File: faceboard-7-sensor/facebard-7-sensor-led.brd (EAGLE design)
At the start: 37 x 91.4 mm, 31 parts, among them Q1 QRE1113, Q2 QRE1113, Q3 QRE1113, Q4 QRE1113, Q5 QRE1113, Q6 QRE1113, Q7 QRE1113, U1 CD4051BE

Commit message: routing
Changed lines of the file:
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@@
 <signal name="C0">
 <contactref element="U1" pad="13"/>
+<wire x1="15.18" y1="7" x2="15.18" y2="19.46894375" width="0.1524" layer="16"/>
+<wire x1="16.6659" y1="20.95484375" x2="15.18" y2="19.46894375" width="0.1524" layer="16"/>
+<wire x1="15.18" y1="43.47" x2="15.18" y2="42.16928125" width="0.1524" layer="16"/>
+<wire x1="15.18" y1="42.16928125" x2="16.6659" y2="40.68338125" width="0.1524" layer="16"/>
+<wire x1="16.6659" y1="40.68338125" x2="16.6659" y2="20.95484375" width="0.1524" layer="16"/>
 <contactref element="Q1" pad="3"/>
 <contactref element="R2" pad="1"/>
 <wire x1="5.515" y1="3.5134" x2="8.5066" y2="3.5134" width="0.1524" layer="1"/>
 <wire x1="8.5066" y1="3.5134" x2="10.1" y2="1.92" width="0.1524" layer="1"/>
-<wire x1="15.18" y1="7" x2="10.1" y2="1.92" width="0.1524" layer="16"/>
-<wire x1="15.18" y1="19.46894375" x2="15.18" y2="7" width="0.1524" layer="16"/>
-<wire x1="16.6659" y1="20.95484375" x2="15.18" y2="19.46894375" width="0.1524" layer="16"/>
-<wire x1="15.18" y1="43.47" x2="15.18" y2="42.16928125" width="0.1524" layer="16"/>
-<wire x1="15.18" y1="42.16928125" x2="16.6659" y2="40.68338125" width="0.1524" layer="16"/>
-<wire x1="16.6659" y1="40.68338125" x2="16.6659" y2="20.95484375" width="0.1524" layer="16"/>
+<wire x1="10.1" y1="1.92" x2="15.18" y2="7" width="0.1524" layer="16"/>
 </signal>
 <signal name="GND">
@@
 </signal>
 <signal name="C1">
+<contactref element="U1" pad="14"/>
+<wire x1="15.18" y1="40.93" x2="15.18" y2="39.62928125" width="0.1524" layer="16"/>
+<wire x1="15.18" y1="39.62928125" x2="16.3611" y2="38.44818125" width="0.1524" layer="16"/>
+<wire x1="16.3611" y1="21.0811" x2="16.3611" y2="38.44818125" width="0.1524" layer="16"/>
 <contactref element="Q2" pad="3"/>
 <contactref element="R4" pad="1"/>
-<contactref element="U1" pad="14"/>
 <wire x1="5.515" y1="17.5334" x2="7.3394" y2="15.709" width="0.1524" layer="1"/>
 <wire x1="7.3394" y1="15.709" x2="7.8682375" y2="15.709" width="0.1524" layer="1"/>
 <wire x1="8.7572375" y1="14.82" x2="10.1" y2="14.82" width="0.1524" layer="1"/>
 <wire x1="7.8682375" y1="15.709" x2="8.7572375" y2="14.82" width="0.1524" layer="1"/>
-<wire x1="15.18" y1="40.93" x2="15.18" y2="39.62928125" width="0.1524" layer="16"/>
-<wire x1="15.18" y1="39.62928125" x2="16.3611" y2="38.44818125" width="0.1524" layer="16"/>
-<wire x1="16.3611" y1="38.44818125" x2="16.3611" y2="21.0811" width="0.1524" layer="16"/>
-<wire x1="16.3611" y1="21.0811" x2="10.1" y2="14.82" width="0.1524" layer="16"/>
+<wire x1="10.1" y1="14.82" x2="16.3611" y2="21.0811" width="0.1524" layer="16"/>
 </signal>
 <signal name="N$5">
@@
 </signal>
 <signal name="C2">
+<contactref element="U1" pad="15"/>
+<wire x1="15.18" y1="38.39" x2="15.18" y2="37.08928125" width="0.1524" layer="16"/>
+<wire x1="15.18" y1="37.08928125" x2="16.0563" y2="36.21298125" width="0.1524" layer="16"/>
+<wire x1="16.0563" y1="36.21298125" x2="16.0563" y2="34" width="0.1524" layer="16"/>
 <contactref element="Q3" pad="3"/>
 <contactref element="R6" pad="1"/>
-<contactref element="U1" pad="15"/>
+<wire x1="16.0563" y1="34" x2="16.0563" y2="33.6763" width="0.1524" layer="16"/>
 <wire x1="5.515" y1="31.5534" x2="9.3484" y2="27.72" width="0.1524" layer="1"/>
 <wire x1="9.3484" y1="27.72" x2="10.1" y2="27.72" width="0.1524" layer="1"/>
-<wire x1="15.18" y1="38.39" x2="15.18" y2="37.08928125" width="0.1524" layer="16"/>
-<wire x1="15.18" y1="37.08928125" x2="16.0563" y2="36.21298125" width="0.1524" layer="16"/>
-<wire x1="16.0563" y1="36.21298125" x2="16.0563" y2="33.6763" width="0.1524" layer="16"/>
-<wire x1="16.0563" y1="33.6763" x2="10.1" y2="27.72" width="0.1524" layer="16"/>
+<wire x1="16.0563" y1="33.6763" x2="16.0563" y2="33.0563" width="0.1524" layer="16"/>
+<wire x1="10.72" y1="27.72" x2="10.1" y2="27.72" width="0.1524" layer="16"/>
+<wire x1="16.0563" y1="33.0563" x2="10.72" y2="27.72" width="0.1524" layer="16"/>
 </signal>
 <signal name="N$7">
@@
 </signal>
 <signal name="C3">
+<contactref element="U1" pad="12"/>
 <contactref element="Q4" pad="3"/>
 <contactref element="R8" pad="1"/>
-<contactref element="U1" pad="12"/>
-<wire x1="5.515" y1="45.5734" x2="10.1" y2="40.9884" width="0.1524" layer="1"/>
-<wire x1="10.1" y1="40.9884" x2="10.1" y2="40.62" width="0.1524" layer="1"/>
 <wire x1="15.18" y1="46.01" x2="10.1" y2="40.93" width="0.1524" layer="16"/>
 <wire x1="10.1" y1="40.93" x2="10.1" y2="40.62" width="0.1524" layer="16"/>
+<wire x1="10.1" y1="40.62" x2="5.515" y2="45.205" width="0.1524" layer="1"/>
+<wire x1="5.515" y1="45.205" x2="5.515" y2="45.5734" width="0.1524" layer="1"/>
 </signal>
 <signal name="N$9">
@@
 <contactref element="Q5" pad="3"/>
 <contactref element="R10" pad="1"/>
-<contactref element="U1" pad="1"/>
 <wire x1="5.515" y1="59.5934" x2="10.1" y2="55.0084" width="0.1524" layer="1"/>
 <wire x1="10.1" y1="55.0084" x2="10.1" y2="53.52" width="0.1524" layer="1"/>
-<wire x1="22.8" y1="35.85" x2="16.0563" y2="42.5937" width="0.1524" layer="16"/>
-<wire x1="10.1" y1="52.32928125" x2="10.1" y2="53" width="0.1524" layer="16"/>
-<wire x1="10.1" y1="53" x2="10.1" y2="53.52" width="0.1524" layer="16"/>
-<wire x1="16.0563" y1="42.5937" x2="16.0563" y2="46" width="0.1524" layer="16"/>
-<wire x1="16.0563" y1="46" x2="16.0563" y2="46.37298125" width="0.1524" layer="16"/>
+<wire x1="10.1" y1="52.0372375" x2="10.1" y2="53.52" width="0.1524" layer="16"/>
+<wire x1="16.0563" y1="42.5937" x2="16.0563" y2="46.37298125" width="0.1524" layer="16"/>
 <wire x1="16.0563" y1="46.37298125" x2="15.54298125" y2="46.8863" width="0.1524" layer="16"/>
 <wire x1="15.54298125" y1="46.8863" x2="15.1733625" y2="46.8863" width="0.1524" layer="16"/>
 <wire x1="15.1733625" y1="46.8863" x2="10.989" y2="51.0706625" width="0.1524" layer="16"/>
 <wire x1="10.989" y1="51.0706625" x2="10.989" y2="51.1482375" width="0.1524" layer="16"/>
-<wire x1="10.1" y1="52.0372375" x2="10.1" y2="52.32928125" width="0.1524" layer="16"/>
 <wire x1="10.989" y1="51.1482375" x2="10.1" y2="52.0372375" width="0.1524" layer="16"/>
+<contactref element="U1" pad="1"/>
+<wire x1="22.8" y1="35.85" x2="16.0563" y2="42.5937" width="0.1524" layer="16"/>
 </signal>
 <signal name="N$11">
@@
 <contactref element="Q6" pad="3"/>
 <contactref element="R12" pad="1"/>
-<contactref element="U1" pad="5"/>
 <wire x1="5.515" y1="73.6134" x2="10.1" y2="69.0284" width="0.1524" layer="1"/>
 <wire x1="10.1" y1="69.0284" x2="10.1" y2="66.42" width="0.1524" layer="1"/>
-<wire x1="22.8" y1="46.01" x2="19.3048" y2="49.5052" width="0.1524" layer="1"/>
 <wire x1="14" y1="56.04928125" x2="14" y2="63" width="0.1524" layer="1"/>
 <wire x1="19.3048" y1="49.5052" x2="19.3048" y2="50.74448125" width="0.1524" layer="1"/>
@@
 <wire x1="14" y1="63" x2="10.58" y2="66.42" width="0.1524" layer="1"/>
 <wire x1="10.58" y1="66.42" x2="10.1" y2="66.42" width="0.1524" layer="1"/>
+<contactref element="U1" pad="5"/>
+<wire x1="22.8" y1="46.01" x2="19.3048" y2="49.5052" width="0.1524" layer="1"/>
 </signal>
 <signal name="N$13">
@@
 </signal>
 <signal name="C6">
-<contactref element="Q7" pad="3"/>
-<contactref element="R14" pad="1"/>
 <contactref element="U1" pad="2"/>
-<wire x1="5.515" y1="87.6334" x2="10.1" y2="83.0484" width="0.1524" layer="1"/>
-<wire x1="10.1" y1="83.0484" x2="10.1" y2="79.32" width="0.1524" layer="1"/>
 <wire x1="22.8" y1="38.39" x2="16.3611" y2="44.8289" width="0.1524" layer="16"/>
 <wire x1="16.3611" y1="44.8289" x2="16.3611" y2="46.4992375" width="0.1524" layer="16"/>
 <wire x1="16" y1="46.8603375" x2="16" y2="47" width="0.1524" layer="16"/>
 <wire x1="16.3611" y1="46.4992375" x2="16" y2="46.8603375" width="0.1524" layer="16"/>
-<wire x1="11.9989" y1="77.4211" x2="10.1" y2="79.32" width="0.1524" layer="16"/>
 <wire x1="16" y1="47" x2="15.3263" y2="47.6737" width="0.1524" layer="16"/>
 <wire x1="15.3263" y1="47.6737" x2="14.81701875" y2="47.6737" width="0.1524" layer="16"/>
 <wire x1="14.81701875" y1="47.6737" x2="11.9989" y2="50.49181875" width="0.1524" layer="16"/>
-<wire x1="11.9989" y1="50.49181875" x2="11.9989" y2="77.4211" width="0.1524" layer="16"/>
+<wire x1="11.9989" y1="50.49181875" x2="11.9989" y2="77" width="0.1524" layer="16"/>
+<contactref element="Q7" pad="3"/>
+<contactref element="R14" pad="1"/>
+<wire x1="5.515" y1="87.6334" x2="10.1" y2="83.0484" width="0.1524" layer="1"/>
+<wire x1="10.1" y1="83.0484" x2="10.1" y2="79.32" width="0.1524" layer="1"/>
+<wire x1="11.9989" y1="77" x2="11.9989" y2="77.4211" width="0.1524" layer="16"/>
+<wire x1="11.9989" y1="77.4211" x2="10.1" y2="79.32" width="0.1524" layer="16"/>
 </signal>
 <signal name="SIG">

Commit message: re-draw schematics
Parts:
- R10: value 10k -> 100k
- SV2: value header -> Output
- SV3: value header -> Input
- moved U1 6.60 mm to (17.0, 39.0), flipped to the bottom
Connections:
- net LEDDIN renamed N$12
- new net N$14: D1.1, D2.1, D3.1
- new net N$15: D4.1
- new net VCC: R1.1, R10.2, R11.1, R12.2, R13.1, R14.2, R2.2, R3.1, R4.2, R5.1, R6.2, R7.1, R8.2, R9.1, SV2.2, SV3.2
- net 5V: no longer R1.1, R10.2, R11.1, R12.2, R13.1, R14.2, R2.2, R3.1, R4.2, R5.1, R6.2, R7.1, R8.2, R9.1, SV2.2, SV3.2
- net GND: no longer D1.1, D2.1, D3.1, D4.1
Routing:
- net 5V: track 127.1 -> 0.00 mm
- net 3V: track 124.5 -> 33.5 mm
- net VCC: track 0.00 -> 88.1 mm
- net C: track 95.5 -> 69.2 mm
- net C4: track 31.1 -> 21.6 mm
- net C6: track 56.7 -> 47.6 mm
- net N$6: track 8.43 -> 0.00 mm
- net N$2: track 8.43 -> 0.00 mm
- net N$8: track 8.43 -> 0.00 mm
- net N$4: track 8.43 -> 0.00 mm
- net N$10: track 8.43 -> 0.00 mm
- net C3: track 14.3 -> 7.16 mm
- net C5: track 35.0 -> 30.1 mm
- net N$12: track 4.69 -> 0.00 mm
- net B: track 97.5 -> 93.7 mm
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
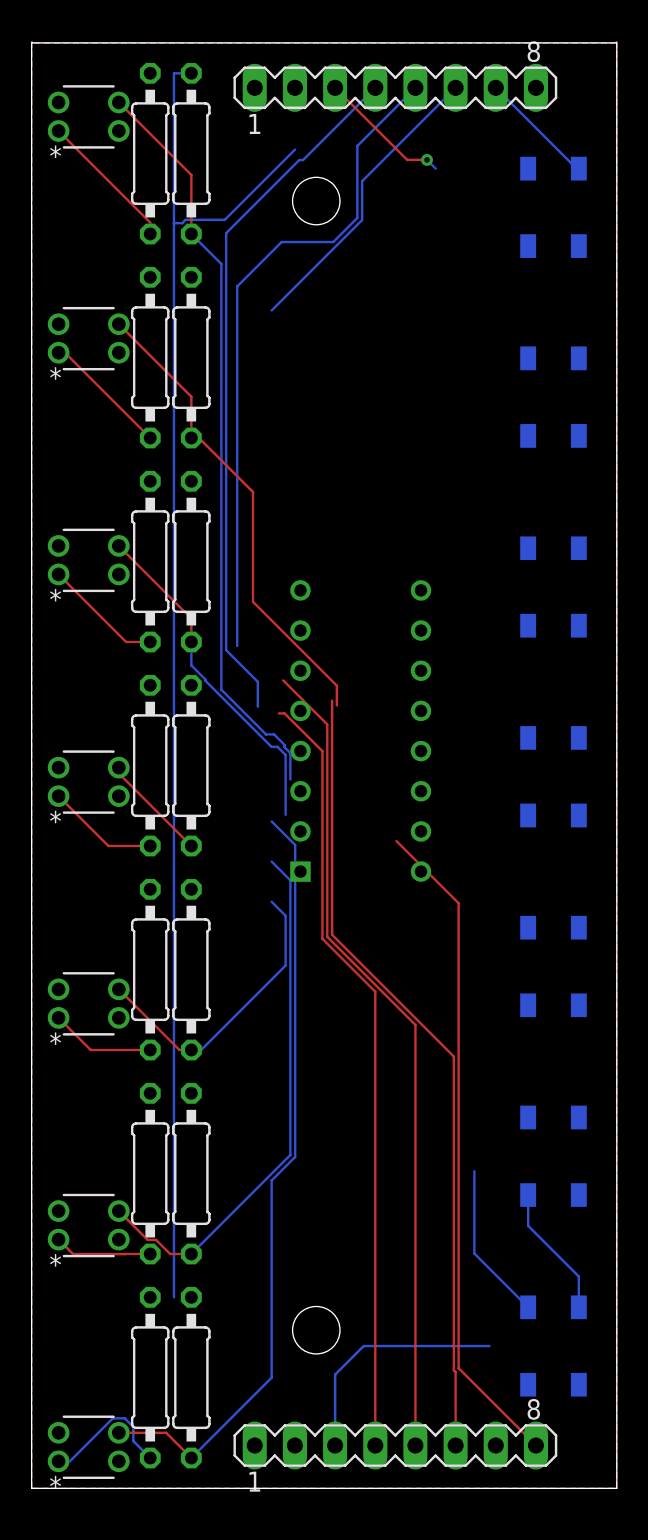
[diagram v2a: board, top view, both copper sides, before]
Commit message: fix vcc net
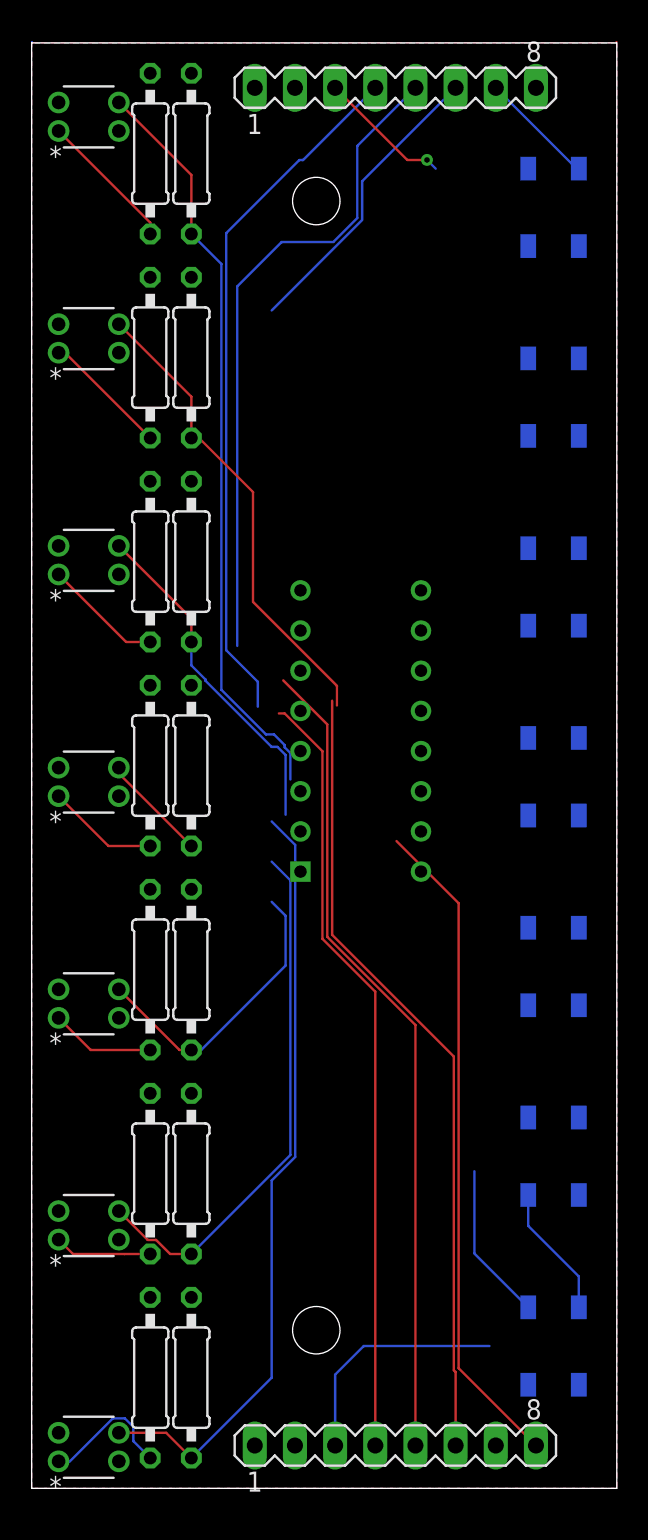
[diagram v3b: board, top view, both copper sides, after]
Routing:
- net VCC: track 88.1 -> 0.00 mm
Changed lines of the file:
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@@
 </signal>
 <signal name="VCC">
+<contactref element="SV3" pad="2"/>
+<contactref element="SV2" pad="2"/>
 <contactref element="R1" pad="1"/>
 <contactref element="R2" pad="2"/>
@@
 <contactref element="R6" pad="2"/>
 <contactref element="R7" pad="1"/>
+<contactref element="R8" pad="2"/>
+<contactref element="R9" pad="1"/>
+<contactref element="R10" pad="2"/>
+<contactref element="R11" pad="1"/>
+<contactref element="R12" pad="2"/>
+<contactref element="R13" pad="1"/>
 <contactref element="R14" pad="2"/>
-<contactref element="R13" pad="1"/>
-<contactref element="R12" pad="2"/>
-<contactref element="R11" pad="1"/>
-<contactref element="R10" pad="2"/>
-<contactref element="R9" pad="1"/>
-<contactref element="R8" pad="2"/>
-<wire x1="9" y1="89.48" x2="10.1" y2="89.48" width="0.1524" layer="16"/>
-<wire x1="9" y1="12.08" x2="9" y2="24.98" width="0.1524" layer="16"/>
-<wire x1="9" y1="24.98" x2="9" y2="37.88" width="0.1524" layer="16"/>
-<wire x1="9" y1="37.88" x2="9" y2="50.78" width="0.1524" layer="16"/>
-<wire x1="9" y1="50.78" x2="9" y2="63.68" width="0.1524" layer="16"/>
-<wire x1="9" y1="63.68" x2="9" y2="76.58" width="0.1524" layer="16"/>
-<wire x1="9" y1="76.58" x2="9" y2="80" width="0.1524" layer="16"/>
-<wire x1="9" y1="80" x2="9" y2="89.48" width="0.1524" layer="16"/>
-<wire x1="9.7317625" y1="80.209" x2="9.5227625" y2="80" width="0.1524" layer="16"/>
-<wire x1="9.5227625" y1="80" x2="9" y2="80" width="0.1524" layer="16"/>
-<wire x1="12.209" y1="80.209" x2="9.7317625" y2="80.209" width="0.1524" layer="16"/>
-<wire x1="16.65" y1="84.65" x2="12.209" y2="80.209" width="0.1524" layer="16"/>
-<contactref element="SV3" pad="2"/>
-<contactref element="SV2" pad="2"/>
-<wire x1="16.65" y1="84.65" x2="16.65" y2="88.56" width="0" layer="19" extent="16-16"/>
-<wire x1="10.1" y1="12.08" x2="9" y2="12.08" width="0" layer="19" extent="16-16"/>
-<wire x1="7.5" y1="12.08" x2="9" y2="12.08" width="0" layer="19" extent="16-16"/>
+<wire x1="10.1" y1="89.48" x2="16.65" y2="88.56" width="0" layer="19" extent="1-1"/>
 <wire x1="7.5" y1="89.48" x2="10.1" y2="89.48" width="0" layer="19" extent="1-1"/>
-<wire x1="10.1" y1="76.58" x2="16.65" y2="84.65" width="0" layer="19" extent="16-16"/>
+<wire x1="10.1" y1="76.58" x2="10.1" y2="89.48" width="0" layer="19" extent="1-1"/>
 <wire x1="7.5" y1="76.58" x2="10.1" y2="76.58" width="0" layer="19" extent="1-1"/>
-<wire x1="16.65" y1="2.71" x2="10.1" y2="12.08" width="0" layer="19" extent="1-1"/>
 <wire x1="10.1" y1="63.68" x2="10.1" y2="76.58" width="0" layer="19" extent="1-1"/>
 <wire x1="7.5" y1="63.68" x2="10.1" y2="63.68" width="0" layer="19" extent="1-1"/>
@@
 <wire x1="10.1" y1="37.88" x2="10.1" y2="50.78" width="0" layer="19" extent="1-1"/>
 <wire x1="7.5" y1="37.88" x2="10.1" y2="37.88" width="0" layer="19" extent="1-1"/>
-<wire x1="10.1" y1="24.98" x2="10.1" y2="12.08" width="0" layer="19" extent="1-1"/>
+<wire x1="10.1" y1="24.98" x2="10.1" y2="37.88" width="0" layer="19" extent="1-1"/>
 <wire x1="7.5" y1="24.98" x2="10.1" y2="24.98" width="0" layer="19" extent="1-1"/>
+<wire x1="10.1" y1="12.08" x2="10.1" y2="24.98" width="0" layer="19" extent="1-1"/>
+<wire x1="7.5" y1="12.08" x2="10.1" y2="12.08" width="0" layer="19" extent="1-1"/>
+<wire x1="16.65" y1="2.71" x2="10.1" y2="12.08" width="0" layer="19" extent="1-1"/>
 </signal>
 <signal name="N$15">

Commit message: add din dout labels
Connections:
- net LEDDOUT renamed DOUT
- net N$12 renamed DIN
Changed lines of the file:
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@@
 <wire x1="31.4" y1="16.6" x2="34.6" y2="13.4" width="0.1524" layer="16"/>
 </signal>
-<signal name="LEDDOUT">
+<signal name="DOUT">
 <contactref element="D7" pad="4"/>
 <contactref element="SV2" pad="7"/>
@@
 <wire x1="34.6" y1="47.45" x2="31.4" y2="54.55" width="0" layer="19" extent="16-16"/>
 </signal>
-<signal name="N$12">
+<signal name="DIN">
 <contactref element="D1" pad="2"/>
 <contactref element="SV3" pad="7"/>

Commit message: tidy
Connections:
- removed net 5V: U1.16
- net VCC: now also U1.16
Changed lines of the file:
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@@
 <contactref element="SV2" pad="8"/>
-</signal>
-<signal name="5V">
-<contactref element="U1" pad="16"/>
 </signal>
 <signal name="A">
@@
 <contactref element="R13" pad="1"/>
 <contactref element="R14" pad="2"/>
+<contactref element="U1" pad="16"/>
 <wire x1="10.1" y1="89.48" x2="16.65" y2="88.56" width="0" layer="19" extent="1-1"/>
 <wire x1="7.5" y1="89.48" x2="10.1" y2="89.48" width="0" layer="19" extent="1-1"/>
@@
 <wire x1="7.5" y1="12.08" x2="10.1" y2="12.08" width="0" layer="19" extent="1-1"/>
 <wire x1="16.65" y1="2.71" x2="10.1" y2="12.08" width="0" layer="19" extent="1-1"/>
+<wire x1="24.62" y1="39" x2="10.1" y2="37.88" width="0" layer="19" extent="1-1"/>
 </signal>
 <signal name="N$15">
